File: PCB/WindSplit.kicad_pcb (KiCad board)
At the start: 2 copper layers, 332.8 x 105.5 mm, 138 parts, among them SW1 SW_Push_45deg, SW10 SW_Push_45deg, SW11 SW_Push_45deg, SW12 SW_Push_45deg, SW13 SW_Push_45deg, SW14 SW_Push_45deg, SW15 SW_Push_45deg, SW16 SW_Push_45deg, SW17 SW_Push_45deg, SW18 SW_Push_45deg, SW19 SW_Push_45deg, SW2 SW_Push_45deg, SW20 SW_Push_45deg, SW21 SW_Push_45deg, SW22 SW_Push_45deg, SW23 SW_Push_45deg, SW24 SW_Push_45deg, SW25 SW_Push_45deg, SW26 SW_Push_45deg, SW27 SW_Push_45deg, SW28 SW_Push_45deg, SW29 SW_Push_45deg, SW3 SW_Push_45deg, SW30 SW_Push_45deg, SW31 SW_Push_45deg, SW32 SW_Push_45deg, SW33 SW_Push_45deg, SW34 SW_Push_45deg, SW35 SW_Push_45deg, SW36 SW_Push_45deg, SW37 SW_Push_45deg, SW38 SW_Push_45deg, SW39 SW_Push_45deg, SW4 SW_Push_45deg, SW40 SW_Push_45deg, SW41 SW_Push_45deg, SW42 SW_Push_45deg, SW43 SW_Push_45deg, SW44 SW_Push_45deg, SW45 SW_Push_45deg, SW46 SW_Push_45deg, SW47 SW_Push_45deg, SW48 SW_Push_45deg, SW49 SW_Push_45deg, SW5 SW_Push_45deg, SW50 SW_Push_45deg, SW51 SW_Push_45deg, SW52 SW_Push_45deg, SW53 SW_Push_45deg, SW54 SW_Push_45deg, SW55 SW_Push_45deg, SW56 SW_Push_45deg, SW57 SW_Push_45deg, SW58 SW_Push_45deg, SW59 SW_Push_45deg, SW6 SW_Push_45deg, SW60 SW_Push_45deg, SW61 SW_Push_45deg, SW62 SW_Push_45deg, SW63 SW_Push_45deg, SW64 SW_Push_45deg, SW65 SW_Push_45deg, SW66 SW_Push_45deg, SW67 SW_Push_45deg, SW68 SW_Push_45deg, SW7 SW_Push_45deg, SW8 SW_Push_45deg, SW9 SW_Push_45deg, U1 Nice_Nano_V2, U2 MCP23017_SP

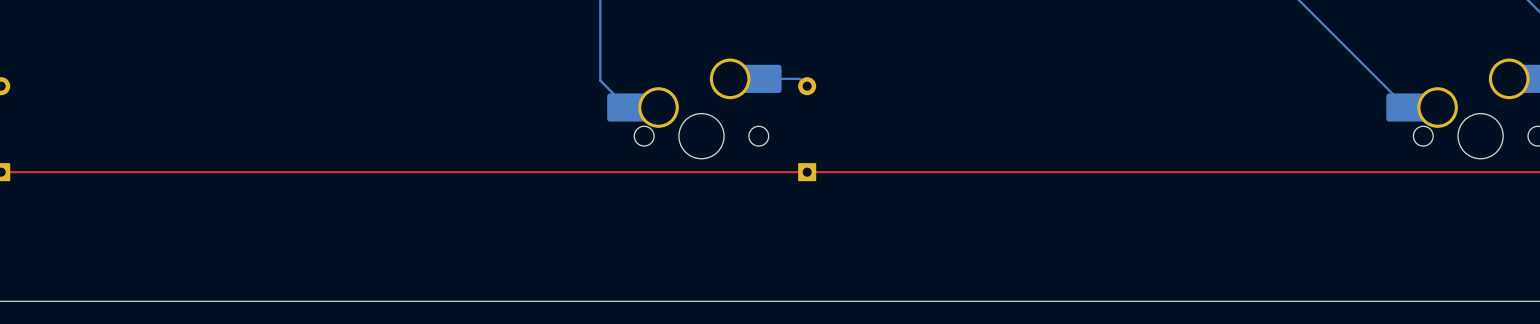
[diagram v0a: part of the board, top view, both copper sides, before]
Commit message: added silkscreen
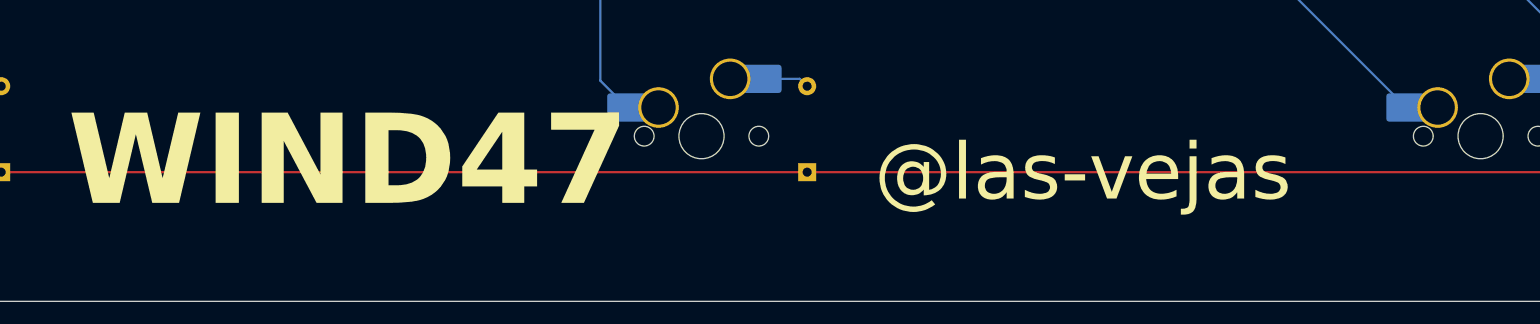
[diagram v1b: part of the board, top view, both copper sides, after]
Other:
- board text added: "@las-vejas"
- board text added: "WIND47"

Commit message: added silk screen
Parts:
- added G***: LOGO, LOGO, F.Cu at (20.5, 109.0)
